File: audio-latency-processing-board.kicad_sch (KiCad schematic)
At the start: 4 parts

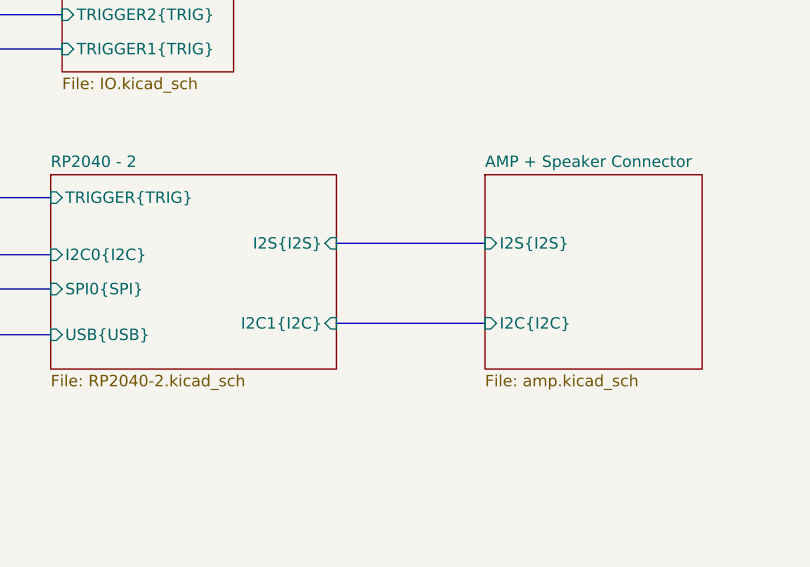
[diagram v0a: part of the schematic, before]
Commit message: [#71986] Remove 1V8 circuits after changing the AMP
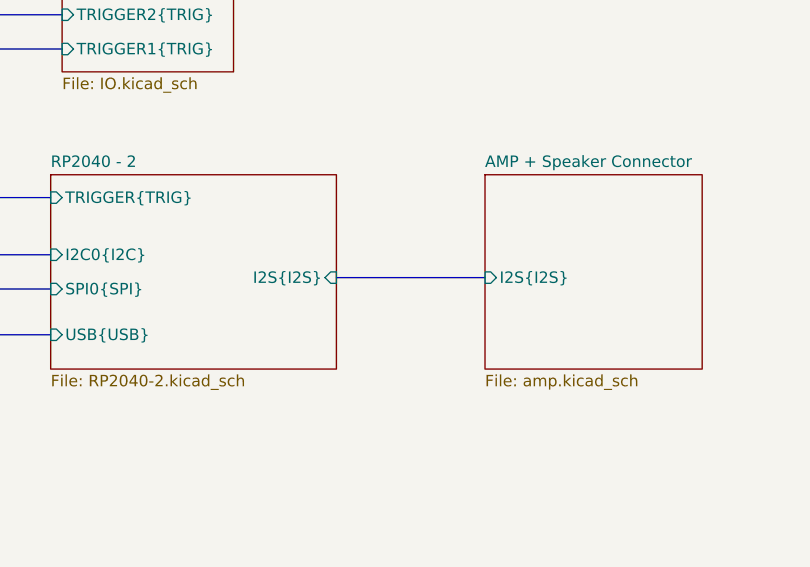
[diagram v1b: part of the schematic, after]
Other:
- sheet AMP + Speaker Connector ports: added none; removed I2C{I2C}
- sheet RP2040 - 2 ports: added none; removed I2C1{I2C}
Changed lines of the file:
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@@
 	(bus
 		(pts
-			(xy 232.41 128.27) (xy 248.92 128.27)
+			(xy 182.88 133.35) (xy 200.66 133.35)
+		)
+		(stroke
+			(width 0)
+			(type default)
+		)
+	)
+	(bus
+		(pts
+			(xy 194.31 106.68) (xy 194.31 123.19)
+		)
+		(stroke
+			(width 0)
+			(type default)
+		)
+	)
+	(bus
+		(pts
+			(xy 190.5 138.43) (xy 182.88 138.43)
+		)
+		(stroke
+			(width 0)
+			(type default)
+		)
+	)
+	(bus
+		(pts
+			(xy 182.88 129.54) (xy 200.66 129.54)
+		)
+		(stroke
+			(width 0)
+			(type default)
+		)
+	)
+	(bus
+		(pts
+			(xy 194.31 138.43) (xy 200.66 138.43)
+		)
+		(stroke
+			(width 0)
+			(type default)
+		)
+	)
+	(bus
+		(pts
+			(xy 190.5 102.87) (xy 201.93 102.87)
+		)
+		(stroke
+			(width 0)
+			(type default)
+		)
+	)
+	(bus
+		(pts
+			(xy 232.41 132.08) (xy 248.92 132.08)
 		)
 		(stroke
@@
 			(type default)
 			(color 241 95 50 1)
-		)
-	)
-	(bus
-		(pts
-			(xy 182.88 133.35) (xy 200.66 133.35)
-		)
-		(stroke
-			(width 0)
-			(type default)
-		)
-	)
-	(bus
-		(pts
-			(xy 232.41 137.16) (xy 248.92 137.16)
-		)
-		(stroke
-			(width 0)
-			(type default)
-		)
-	)
-	(bus
-		(pts
-			(xy 194.31 106.68) (xy 194.31 123.19)
-		)
-		(stroke
-			(width 0)
-			(type default)
-		)
-	)
-	(bus
-		(pts
-			(xy 190.5 138.43) (xy 182.88 138.43)
-		)
-		(stroke
-			(width 0)
-			(type default)
-		)
-	)
-	(bus
-		(pts
-			(xy 182.88 129.54) (xy 200.66 129.54)
-		)
-		(stroke
-			(width 0)
-			(type default)
-		)
-	)
-	(bus
-		(pts
-			(xy 194.31 138.43) (xy 200.66 138.43)
-		)
-		(stroke
-			(width 0)
-			(type default)
-		)
-	)
-	(bus
-		(pts
-			(xy 190.5 102.87) (xy 201.93 102.87)
-		)
-		(stroke
-			(width 0)
-			(type default)
 		)
 	)
@@
 			)
 		)
-		(pin "I2C{I2C}" input
-			(at 248.92 137.16 180)
-			(effects
-				(font
-					(size 1.27 1.27)
-				)
-				(justify left)
-			)
-		)
 		(pin "I2S{I2S}" input
-			(at 248.92 128.27 180)
+			(at 248.92 132.08 180)
 			(effects
 				(font
@@
 			)
 		)
-		(pin "I2C1{I2C}" input
-			(at 232.41 137.16 0)
-			(effects
-				(font
-					(size 1.27 1.27)
-				)
-				(justify right)
-			)
-		)
 		(pin "I2S{I2S}" input
-			(at 232.41 128.27 0)
-			(effects
-				(font
+			(at 232.41 132.08 0)
+			(effects
+				(font
